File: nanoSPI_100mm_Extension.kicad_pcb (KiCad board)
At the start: 2 copper layers, 5.7 x 105.5 mm, 4 parts, among them J1 FPC contacts 0.3mm, U1 MA735GGU-Z

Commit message: Finished basic design
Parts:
- removed C1: 1uF, Capacitor_SMD:C_0402_1005Metric
- removed C2: 0.1uF, Capacitor_SMD:C_0402_1005Metric
- removed U1: MA735GGU-Z, MA730:UTQFN-14_MA735_MNP
- added J2: FPC 0.3mm Aces 51688-0070M, custom_Connector:fpc_7pin_0.3mm_connector Aces, B.Cu at (152.8, 132.5)
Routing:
- net GND: track 203.9 -> 212.7 mm, vias 3 -> 2
- net +3V3: track 110.6 -> 103.4 mm, vias 2 -> 1
- net /MISO: track 100.7 -> 104.5 mm, vias 0 -> 1
- net /CS: track 99.7 -> 103.2 mm, vias 0 -> 1
- net /MOSI: track 101.4 -> 103.1 mm, vias 0 -> 1
- net /SCK: vias 0 -> 1
- removed copper zone on B.Cu, net GND
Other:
- board size 5.7 x 105.5 mm -> 3.9 x 105.2 mm
- board text removed: "MA735 Encoder ${REVISION}"
- board text removed: "https://github.com/techy-robot/CACKLE-nanoSPI-MA735_magnetic_encoder"

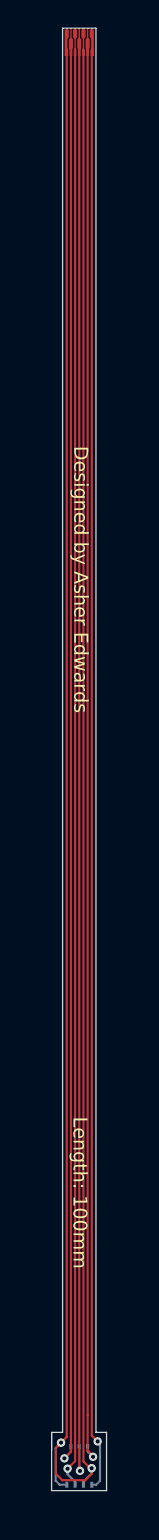
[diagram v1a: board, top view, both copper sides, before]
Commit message: Rounded tracks
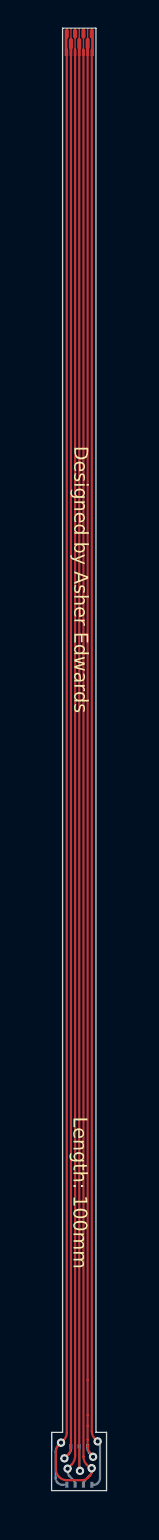
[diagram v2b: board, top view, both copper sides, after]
